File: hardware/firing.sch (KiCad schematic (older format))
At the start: 82 parts, among them IC301 TPS92512, P301 1, P302 2, P303 3, P304 4, P305 5, P306 6, P307 7, P308 8, P309 9, P310 10, P311 11, P312 12, P313 13, P314 14, P315 15, P316 16, P317 17, P318 18, P319 19, P320 20, P321 21, P322 22, P323 23, P324 24, P325 25, P326 26, P327 27, P328 28, P329 29, P330 30, Q301 NTR4501NT1G, Q302 NTR4501NT1G, Q303 NTR4501NT1G, Q304 NTR4501NT1G, Q305 NTR4501NT1G, Q306 NTR4501NT1G, Q307 NTR4501NT1G, Q308 NTR4501NT1G, Q309 NTR4501NT1G, Q310 NTR4501NT1G, Q311 NTR4501NT1G, Q312 NTR4501NT1G, Q313 NTR4501NT1G, Q314 NTR4501NT1G, Q315 NTR4501NT1G, Q316 NTR4501NT1G, Q317 NTR4501NT1G, Q318 NTR4501NT1G, Q319 NTR4501NT1G, Q320 NTR4501NT1G, Q321 NTR4501NT1G, Q322 NTR4501NT1G, Q323 NTR4501NT1G, Q324 NTR4501NT1G, Q325 NTR4501NT1G, Q326 NTR4501NT1G, Q327 NTR4501NT1G, Q328 NTR4501NT1G, Q329 NTR4501NT1G, Q330 NTR4501NT1G

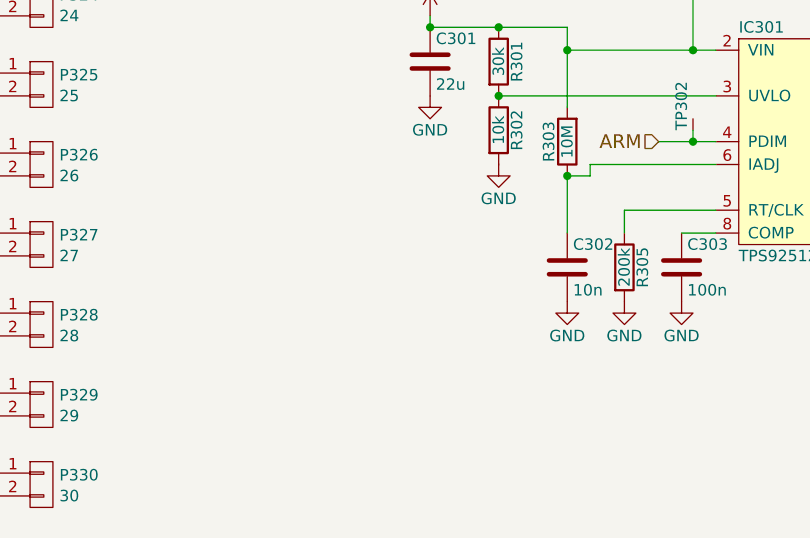
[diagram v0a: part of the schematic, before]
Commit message: add pulldown to ARM line
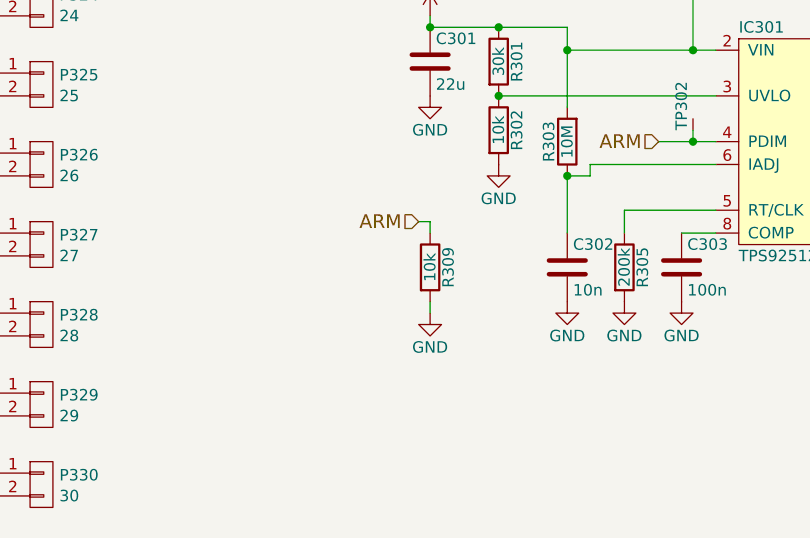
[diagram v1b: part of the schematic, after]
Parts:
- added R309: 10k, agg:0603, symbol R
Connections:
- net ARM: now also R309.1
- net GND: now also R309.2
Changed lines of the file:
@@
 GND
 $Comp
-L +6V #PWR081
+L +6V #PWR305
 U 1 1 57F2318E
 P 6650 1400
-F 0 "#PWR081" H 6650 1250 50  0001 C CNN
+F 0 "#PWR305" H 6650 1250 50  0001 C CNN
 F 1 "+6V" H 6650 1540 50  0000 C CNN
 F 2 "" H 6650 1400 50  0000 C CNN
@@
 $EndComp
 $Comp
-L GND #PWR082
+L GND #PWR306
 U 1 1 57F232B2
 P 6650 1600
-F 0 "#PWR082" H 6650 1350 50  0001 C CNN
+F 0 "#PWR306" H 6650 1350 50  0001 C CNN
 F 1 "GND" H 6650 1450 50  0000 C CNN
 F 2 "" H 6650 1600 50  0000 C CNN
@@
 $EndComp
 $Comp
-L 3v3 #PWR083
+L 3v3 #PWR307
 U 1 1 57F163DE
 P 6700 2500
-F 0 "#PWR083" H 6700 2610 50  0001 L CNN
+F 0 "#PWR307" H 6700 2610 50  0001 L CNN
 F 1 "3v3" H 6700 2590 50  0000 C CNN
 F 2 "" H 6700 2500 60  0001 C CNN
@@
 BUS
 $Comp
-L 3v3 #PWR084
+L 3v3 #PWR311
 U 1 1 57F1767D
 P 7800 2500
-F 0 "#PWR084" H 7800 2610 50  0001 L CNN
+F 0 "#PWR311" H 7800 2610 50  0001 L CNN
 F 1 "3v3" H 7800 2590 50  0000 C CNN
 F 2 "" H 7800 2500 60  0001 C CNN
@@
 $EndComp
 $Comp
-L +6V #PWR085
+L +6V #PWR301
 U 1 1 57F2A1FC
 P 6300 4500
-F 0 "#PWR085" H 6300 4350 50  0001 C CNN
+F 0 "#PWR301" H 6300 4350 50  0001 C CNN
 F 1 "+6V" H 6300 4640 50  0000 C CNN
 F 2 "" H 6300 4500 50  0000 C CNN
@@
 $EndComp
 $Comp
-L GND #PWR086
+L GND #PWR302
 U 1 1 57F2A430
 P 6300 4850
-F 0 "#PWR086" H 6300 4600 50  0001 C CNN
+F 0 "#PWR302" H 6300 4600 50  0001 C CNN
 F 1 "GND" H 6300 4700 50  0000 C CNN
 F 2 "" H 6300 4850 50  0000 C CNN
@@
 $EndComp
 $Comp
-L GND #PWR087
+L GND #PWR304
 U 1 1 57F2A895
 P 6600 5150
-F 0 "#PWR087" H 6600 4900 50  0001 C CNN
+F 0 "#PWR304" H 6600 4900 50  0001 C CNN
 F 1 "GND" H 6600 5000 50  0000 C CNN
 F 2 "" H 6600 5150 50  0000 C CNN
@@
 $EndComp
 $Comp
-L GND #PWR088
+L GND #PWR308
 U 1 1 57F2B6DE
 P 6900 5750
-F 0 "#PWR088" H 6900 5500 50  0001 C CNN
+F 0 "#PWR308" H 6900 5500 50  0001 C CNN
 F 1 "GND" H 6900 5600 50  0000 C CNN
 F 2 "" H 6900 5750 50  0000 C CNN
@@
 $EndComp
 $Comp
-L GND #PWR089
+L GND #PWR309
 U 1 1 57F2B991
 P 7150 5750
-F 0 "#PWR089" H 7150 5500 50  0001 C CNN
+F 0 "#PWR309" H 7150 5500 50  0001 C CNN
 F 1 "GND" H 7150 5600 50  0000 C CNN
 F 2 "" H 7150 5750 50  0000 C CNN
@@
 $EndComp
 $Comp
-L GND #PWR090
+L GND #PWR310
 U 1 1 57F2BEB6
 P 7400 5750
-F 0 "#PWR090" H 7400 5500 50  0001 C CNN
+F 0 "#PWR310" H 7400 5500 50  0001 C CNN
 F 1 "GND" H 7400 5600 50  0000 C CNN
 F 2 "" H 7400 5750 50  0000 C CNN
@@
 $EndComp
 $Comp
-L GND #PWR091
+L GND #PWR313
 U 1 1 57F2D81B
 P 8950 5600
-F 0 "#PWR091" H 8950 5350 50  0001 C CNN
+F 0 "#PWR313" H 8950 5350 50  0001 C CNN
 F 1 "GND" H 8950 5450 50  0000 C CNN
 F 2 "" H 8950 5600 50  0000 C CNN
@@
 $EndComp
 $Comp
-L GND #PWR092
+L GND #PWR312
 U 1 1 57F2D90D
 P 8650 5650
-F 0 "#PWR092" H 8650 5400 50  0001 C CNN
+F 0 "#PWR312" H 8650 5400 50  0001 C CNN
 F 1 "GND" H 8650 5500 50  0000 C CNN
 F 2 "" H 8650 5650 50  0000 C CNN
@@
 $EndComp
 $Comp
-L GND #PWR093
+L GND #PWR314
 U 1 1 57F316A5
 P 10000 5400
-F 0 "#PWR093" H 10000 5150 50  0001 C CNN
+F 0 "#PWR314" H 10000 5150 50  0001 C CNN
 F 1 "GND" H 10000 5250 50  0000 C CNN
 F 2 "" H 10000 5400 50  0000 C CNN
@@
 	8050 2750 8050 2800
 Connection ~ 8050 2800
+$Comp
+L R R309
+U 1 1 5801B678
+P 6300 5600
+F 0 "R309" V 6380 5600 50  0000 C CNN
+F 1 "10k" V 6300 5600 50  0000 C CNN
+F 2 "agg:0603" V 6230 5600 50  0001 C CNN
+F 3 "http://www.farnell.com/datasheets/1911175.pdf" H 6300 5600 50  0001 C CNN
+F 4 "2303192" H 6300 5600 60  0001 C CNN "Farnell"
+	1    6300 5600
+	1    0    0    -1
+$EndComp
+Text HLabel 6250 5400 0    60   Input ~ 0
+ARM
+Wire Wire Line
+	6250 5400 6300 5400
+Wire Wire Line
+	6300 5400 6300 5450
+$Comp
+L GND #PWR303
+U 1 1 5801BD9E
+P 6300 5800
+F 0 "#PWR303" H 6300 5550 50  0001 C CNN
+F 1 "GND" H 6300 5650 50  0000 C CNN
+F 2 "" H 6300 5800 50  0000 C CNN
+F 3 "" H 6300 5800 50  0000 C CNN
+	1    6300 5800
+	1    0    0    -1
+$EndComp
+Wire Wire Line
+	6300 5750 6300 5800
 $EndSCHEMATC

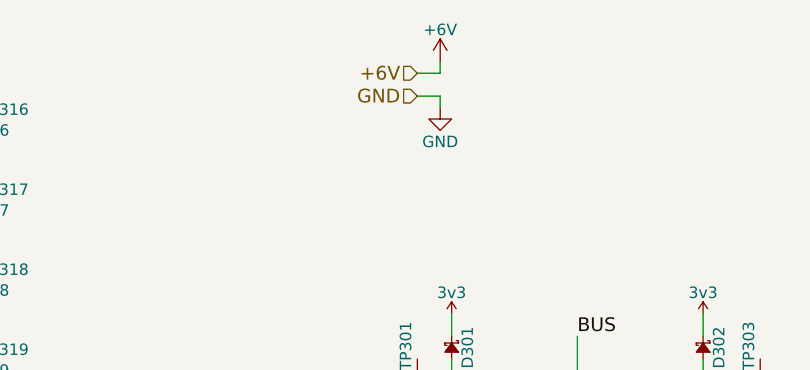
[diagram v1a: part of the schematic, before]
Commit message: remove power schematic sheet pins
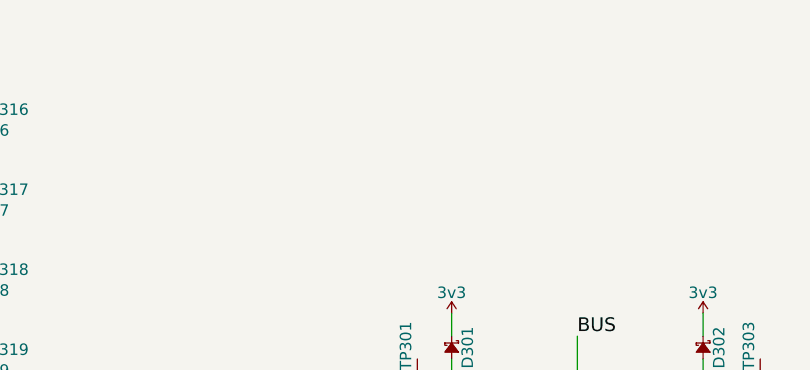
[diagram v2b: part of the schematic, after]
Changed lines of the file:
@@
 Text HLabel 3950 6400 0    60   Input ~ 0
 CH30
-Text HLabel 6550 1450 0    60   Input ~ 0
-+6V
-Text HLabel 6550 1550 0    60   Input ~ 0
-GND
-$Comp
-L +6V #PWR305
-U 1 1 57F2318E
-P 6650 1400
-F 0 "#PWR305" H 6650 1250 50  0001 C CNN
-F 1 "+6V" H 6650 1540 50  0000 C CNN
-F 2 "" H 6650 1400 50  0000 C CNN
-F 3 "" H 6650 1400 50  0000 C CNN
-	1    6650 1400
-	1    0    0    -1
-$EndComp
-$Comp
-L GND #PWR306
-U 1 1 57F232B2
-P 6650 1600
-F 0 "#PWR306" H 6650 1350 50  0001 C CNN
-F 1 "GND" H 6650 1450 50  0000 C CNN
-F 2 "" H 6650 1600 50  0000 C CNN
-F 3 "" H 6650 1600 50  0000 C CNN
-	1    6650 1600
-	1    0    0    -1
-$EndComp
 Text Label 2450 1650 2    60   ~ 0
 BUS
@@
 $EndComp
 $Comp
-L 3v3 #PWR307
+L 3v3 #PWR081
 U 1 1 57F163DE
 P 6700 2500
-F 0 "#PWR307" H 6700 2610 50  0001 L CNN
+F 0 "#PWR081" H 6700 2610 50  0001 L CNN
 F 1 "3v3" H 6700 2590 50  0000 C CNN
 F 2 "" H 6700 2500 60  0001 C CNN
@@
 BUS
 $Comp
-L 3v3 #PWR311
+L 3v3 #PWR082
 U 1 1 57F1767D
 P 7800 2500
-F 0 "#PWR311" H 7800 2610 50  0001 L CNN
+F 0 "#PWR082" H 7800 2610 50  0001 L CNN
 F 1 "3v3" H 7800 2590 50  0000 C CNN
 F 2 "" H 7800 2500 60  0001 C CNN
@@
 $EndComp
 $Comp
-L +6V #PWR301
+L +6V #PWR083
 U 1 1 57F2A1FC
 P 6300 4500
-F 0 "#PWR301" H 6300 4350 50  0001 C CNN
+F 0 "#PWR083" H 6300 4350 50  0001 C CNN
 F 1 "+6V" H 6300 4640 50  0000 C CNN
 F 2 "" H 6300 4500 50  0000 C CNN
@@
 $EndComp
 $Comp
-L GND #PWR302
+L GND #PWR084
 U 1 1 57F2A430
 P 6300 4850
-F 0 "#PWR302" H 6300 4600 50  0001 C CNN
+F 0 "#PWR084" H 6300 4600 50  0001 C CNN
 F 1 "GND" H 6300 4700 50  0000 C CNN
 F 2 "" H 6300 4850 50  0000 C CNN
@@
 $EndComp
 $Comp
-L GND #PWR304
+L GND #PWR085
 U 1 1 57F2A895
 P 6600 5150
-F 0 "#PWR304" H 6600 4900 50  0001 C CNN
+F 0 "#PWR085" H 6600 4900 50  0001 C CNN
 F 1 "GND" H 6600 5000 50  0000 C CNN
 F 2 "" H 6600 5150 50  0000 C CNN
@@
 $EndComp
 $Comp
-L GND #PWR308
+L GND #PWR086
 U 1 1 57F2B6DE
 P 6900 5750
-F 0 "#PWR308" H 6900 5500 50  0001 C CNN
+F 0 "#PWR086" H 6900 5500 50  0001 C CNN
 F 1 "GND" H 6900 5600 50  0000 C CNN
 F 2 "" H 6900 5750 50  0000 C CNN
@@
 $EndComp
 $Comp
-L GND #PWR309
+L GND #PWR087
 U 1 1 57F2B991
 P 7150 5750
-F 0 "#PWR309" H 7150 5500 50  0001 C CNN
+F 0 "#PWR087" H 7150 5500 50  0001 C CNN
 F 1 "GND" H 7150 5600 50  0000 C CNN
 F 2 "" H 7150 5750 50  0000 C CNN
@@
 $EndComp
 $Comp
-L GND #PWR310
+L GND #PWR088
 U 1 1 57F2BEB6
 P 7400 5750
-F 0 "#PWR310" H 7400 5500 50  0001 C CNN
+F 0 "#PWR088" H 7400 5500 50  0001 C CNN
 F 1 "GND" H 7400 5600 50  0000 C CNN
 F 2 "" H 7400 5750 50  0000 C CNN
@@
 $EndComp
 $Comp
-L GND #PWR313
+L GND #PWR089
 U 1 1 57F2D81B
 P 8950 5600
-F 0 "#PWR313" H 8950 5350 50  0001 C CNN
+F 0 "#PWR089" H 8950 5350 50  0001 C CNN
 F 1 "GND" H 8950 5450 50  0000 C CNN
 F 2 "" H 8950 5600 50  0000 C CNN
@@
 $EndComp
 $Comp
-L GND #PWR312
+L GND #PWR090
 U 1 1 57F2D90D
 P 8650 5650
-F 0 "#PWR312" H 8650 5400 50  0001 C CNN
+F 0 "#PWR090" H 8650 5400 50  0001 C CNN
 F 1 "GND" H 8650 5500 50  0000 C CNN
 F 2 "" H 8650 5650 50  0000 C CNN
@@
 $EndComp
 $Comp
-L GND #PWR314
+L GND #PWR091
 U 1 1 57F316A5
 P 10000 5400
-F 0 "#PWR314" H 10000 5150 50  0001 C CNN
+F 0 "#PWR091" H 10000 5150 50  0001 C CNN
 F 1 "GND" H 10000 5250 50  0000 C CNN
 F 2 "" H 10000 5400 50  0000 C CNN
@@
 Wire Wire Line
 	4400 6600 4150 6600
-Wire Wire Line
-	6650 1400 6650 1450
-Wire Wire Line
-	6650 1450 6550 1450
-Wire Wire Line
-	6550 1550 6650 1550
-Wire Wire Line
-	6650 1550 6650 1600
 Wire Wire Line
 	6450 2800 6850 2800
@@
 	6300 5400 6300 5450
 $Comp
-L GND #PWR303
+L GND #PWR092
 U 1 1 5801BD9E
 P 6300 5800
-F 0 "#PWR303" H 6300 5550 50  0001 C CNN
+F 0 "#PWR092" H 6300 5550 50  0001 C CNN
 F 1 "GND" H 6300 5650 50  0000 C CNN
 F 2 "" H 6300 5800 50  0000 C CNN
